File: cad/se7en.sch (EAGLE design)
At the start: 67 parts, among them CN1 MICROSD-EJECT, CN3 DO NOT PLACE, CN4 DO NOT PLACE, CN5 DO NOT PLACE, CN8 HEADER-1X2-THM, Q1 FDC6392S, SW1 SWITCHKMR211, SW2 SWITCHKMR211, U1 ATSAMS70, U2 MCP73831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

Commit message: tweak
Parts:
- CN2: device adafruit:JST_2PIN-SMT-RA -> jaw:JST_2PIN-SMT-RA
- USB1: value CON-USB-F-MICRO-B -> USB-F-B-MICRO-B-192; device dp_devices:CON-USB-F-MICRO-B -> jaw:USB-F-B-MICRO-B-192
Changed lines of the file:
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@@
 <grid distance="0.1" unitdist="inch" unit="inch" style="lines" multiple="1" display="no" altdistance="0.01" altunitdist="inch" altunit="inch"/>
 <layers>
-<layer number="1" name="Top" color="4" fill="1" visible="no" active="no"/>
-<layer number="2" name="Route2" color="6" fill="1" visible="no" active="no"/>
-<layer number="3" name="Route3" color="4" fill="3" visible="no" active="no"/>
-<layer number="14" name="Route14" color="1" fill="6" visible="no" active="no"/>
-<layer number="15" name="Route15" color="13" fill="1" visible="no" active="no"/>
-<layer number="16" name="Bottom" color="1" fill="1" visible="no" active="no"/>
-<layer number="17" name="Pads" color="2" fill="1" visible="no" active="no"/>
-<layer number="18" name="Vias" color="2" fill="1" visible="no" active="no"/>
-<layer number="19" name="Unrouted" color="6" fill="1" visible="no" active="no"/>
-<layer number="20" name="Dimension" color="15" fill="1" visible="no" active="no"/>
-<layer number="21" name="tPlace" color="7" fill="1" visible="no" active="no"/>
-<layer number="22" name="bPlace" color="7" fill="1" visible="no" active="no"/>
-<layer number="23" name="tOrigins" color="15" fill="1" visible="no" active="no"/>
-<layer number="24" name="bOrigins" color="15" fill="1" visible="no" active="no"/>
-<layer number="25" name="tNames" color="7" fill="1" visible="no" active="no"/>
-<layer number="26" name="bNames" color="7" fill="1" visible="no" active="no"/>
-<layer number="27" name="tValues" color="7" fill="1" visible="no" active="no"/>
-<layer number="28" name="bValues" color="7" fill="1" visible="no" active="no"/>
+<layer number="1" name="Top" color="4" fill="1" visible="yes" active="no"/>
+<layer number="2" name="Route2" color="6" fill="1" visible="yes" active="no"/>
+<layer number="3" name="Route3" color="4" fill="3" visible="yes" active="no"/>
+<layer number="14" name="Route14" color="1" fill="6" visible="yes" active="no"/>
+<layer number="15" name="Route15" color="13" fill="1" visible="yes" active="no"/>
+<layer number="16" name="Bottom" color="1" fill="1" visible="yes" active="no"/>
+<layer number="17" name="Pads" color="2" fill="1" visible="yes" active="no"/>
+<layer number="18" name="Vias" color="2" fill="1" visible="yes" active="no"/>
+<layer number="19" name="Unrouted" color="6" fill="1" visible="yes" active="no"/>
+<layer number="20" name="Dimension" color="15" fill="1" visible="yes" active="no"/>
+<layer number="21" name="tPlace" color="7" fill="1" visible="yes" active="no"/>
+<layer number="22" name="bPlace" color="7" fill="1" visible="yes" active="no"/>
+<layer number="23" name="tOrigins" color="15" fill="1" visible="yes" active="no"/>
+<layer number="24" name="bOrigins" color="15" fill="1" visible="yes" active="no"/>
+<layer number="25" name="tNames" color="7" fill="1" visible="yes" active="no"/>
+<layer number="26" name="bNames" color="7" fill="1" visible="yes" active="no"/>
+<layer number="27" name="tValues" color="7" fill="1" visible="yes" active="no"/>
+<layer number="28" name="bValues" color="7" fill="1" visible="yes" active="no"/>
 <layer number="29" name="tStop" color="7" fill="3" visible="no" active="no"/>
 <layer number="30" name="bStop" color="7" fill="6" visible="no" active="no"/>
@@
 <layer number="35" name="tGlue" color="7" fill="4" visible="no" active="no"/>
 <layer number="36" name="bGlue" color="7" fill="5" visible="no" active="no"/>
-<layer number="37" name="tTest" color="7" fill="1" visible="no" active="no"/>
-<layer number="38" name="bTest" color="7" fill="1" visible="no" active="no"/>
+<layer number="37" name="tTest" color="7" fill="1" visible="yes" active="no"/>
+<layer number="38" name="bTest" color="7" fill="1" visible="yes" active="no"/>
 <layer number="39" name="tKeepout" color="4" fill="11" visible="no" active="no"/>
 <layer number="40" name="bKeepout" color="1" fill="11" visible="no" active="no"/>
@@
 <layer number="44" name="Drills" color="7" fill="1" visible="no" active="no"/>
 <layer number="45" name="Holes" color="7" fill="1" visible="no" active="no"/>
-<layer number="46" name="Milling" color="3" fill="1" visible="no" active="no"/>
-<layer number="47" name="Measures" color="7" fill="1" visible="no" active="no"/>
-<layer number="48" name="Document" color="7" fill="1" visible="no" active="no"/>
-<layer number="49" name="Reference" color="7" fill="1" visible="no" active="no"/>
-<layer number="50" name="dxf" color="7" fill="1" visible="no" active="no"/>
-<layer number="51" name="tDocu" color="7" fill="1" visible="no" active="no"/>
-<layer number="52" name="bDocu" color="7" fill="1" visible="no" active="no"/>
-<layer number="53" name="tGND_GNDA" color="7" fill="1" visible="no" active="no"/>
-<layer number="54" name="bGND_GNDA" color="7" fill="1" visible="no" active="no"/>
-<layer number="56" name="wert" color="7" fill="1" visible="no" active="no"/>
-<layer number="57" name="tCAD" color="7" fill="1" visible="no" active="no"/>
-<layer number="59" name="tCarbon" color="7" fill="1" visible="no" active="no"/>
-<layer number="60" name="bCarbon" color="7" fill="1" visible="no" active="no"/>
+<layer number="46" name="Milling" color="3" fill="1" visible="yes" active="no"/>
+<layer number="47" name="Measures" color="7" fill="1" visible="yes" active="no"/>
+<layer number="48" name="Document" color="7" fill="1" visible="yes" active="no"/>
+<layer number="49" name="Reference" color="7" fill="1" visible="yes" active="no"/>
+<layer number="50" name="dxf" color="7" fill="1" visible="yes" active="no"/>
+<layer number="51" name="tDocu" color="7" fill="1" visible="yes" active="no"/>
+<layer number="52" name="bDocu" color="7" fill="1" visible="yes" active="no"/>
+<layer number="53" name="tGND_GNDA" color="7" fill="1" visible="yes" active="no"/>
+<layer number="54" name="bGND_GNDA" color="7" fill="1" visible="yes" active="no"/>
+<layer number="56" name="wert" color="7" fill="1" visible="yes" active="no"/>
+<layer number="57" name="tCAD" color="7" fill="1" visible="yes" active="no"/>
+<layer number="59" name="tCarbon" color="7" fill="1" visible="yes" active="no"/>
+<layer number="60" name="bCarbon" color="7" fill="1" visible="yes" active="no"/>
 <layer number="90" name="Modules" color="5" fill="1" visible="yes" active="yes"/>
 <layer number="91" name="Nets" color="2" fill="1" visible="yes" active="yes"/>
@@
 <part name="C17" library="jaw" deviceset="C" device="-0402" value=".1u"/>
 <part name="C18" library="jaw" deviceset="C" device="-0402" value=".1u"/>
-<part name="USB1" library="dp_devices" deviceset="CON-USB-F" device="-MICRO-B"/>
+<part name="USB1" library="jaw" deviceset="USB-F-B" device="-MICRO-B-192"/>
 <part name="GND10" library="jaw" deviceset="PWR-GND" device=""/>
 <part name="CN1" library="jaw" deviceset="MICROSD" device="-EJECT"/>
 <part name="C19" library="jaw" deviceset="C" device="-0402" value=".1u"/>
-<part name="CN2" library="adafruit" deviceset="JST_2PIN" device="-SMT-RA"/>
+<part name="CN2" library="jaw" deviceset="JST_2PIN" device="-SMT-RA"/>
 <part name="CN5" library="adafruit" deviceset="PINHD-2X20" device="" value="DO NOT PLACE"/>
 <part name="CN3" library="jaw" deviceset="HEADER-3X2" device="-POGO" value="DO NOT PLACE"/>

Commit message: usb improve Zd
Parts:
- CN8: value HEADER-1X2-THM -> HEADER-1X2M254; device jaw:HEADER-1X2-THM -> jaw:HEADER-1X2M254
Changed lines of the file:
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@@
 <part name="LED2" library="jaw" deviceset="LED" device="" value="green"/>
 <part name="LED3" library="jaw" deviceset="LED" device="" value="orange"/>
-<part name="CN8" library="jaw" deviceset="HEADER-1X2" device="-THM"/>
+<part name="CN8" library="jaw" deviceset="HEADER-1X2" device="M254" value="HEADER-1X2M254"/>
 </parts>
 <sheets>

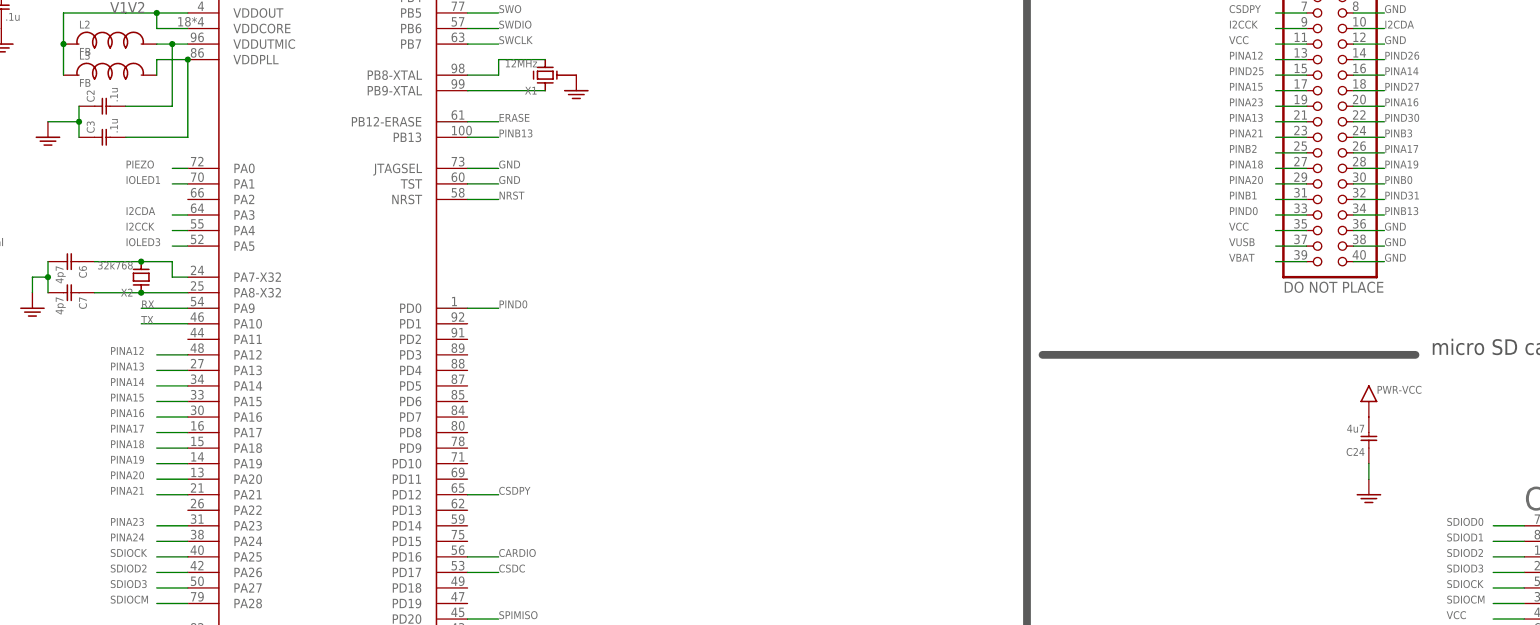
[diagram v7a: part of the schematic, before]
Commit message: drop vbat pins, add more io
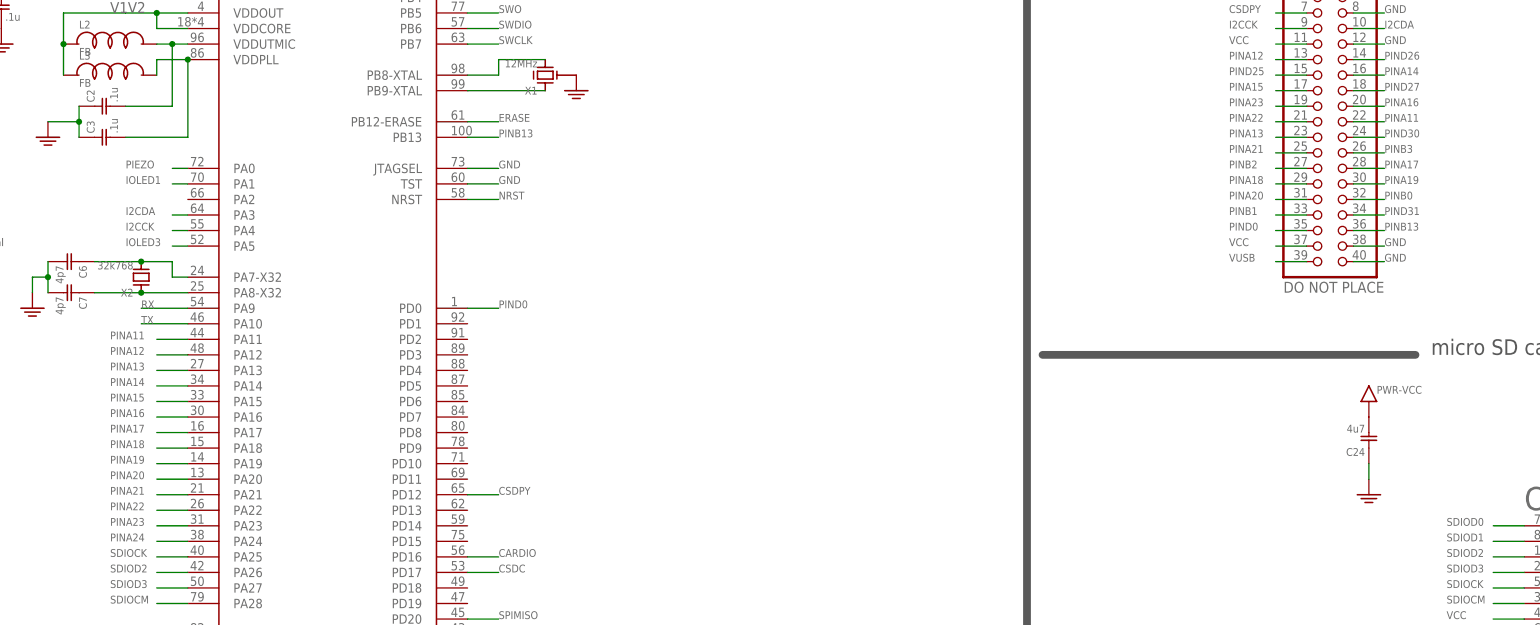
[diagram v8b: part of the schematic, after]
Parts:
- CN8: value HEADER-1X2M254 -> DO NOT PLACE
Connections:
- new net PINA11: CN5.22, U1.PA11
- new net PINA22: CN5.21, U1.PA22
- net GND: no longer CN5.36
- net PINA13: now also CN5.23; no longer CN5.21
- net PINA17: now also CN5.28; no longer CN5.26
- net PINA18: now also CN5.29; no longer CN5.27
- net PINA19: now also CN5.30; no longer CN5.28
- net PINA20: now also CN5.31; no longer CN5.29
- net PINA21: now also CN5.25; no longer CN5.23
- net PINB0: now also CN5.32; no longer CN5.30
- net PINB1: now also CN5.33; no longer CN5.31
- net PINB13: now also CN5.36; no longer CN5.34
- net PINB2: now also CN5.27; no longer CN5.25
- net PINB3: now also CN5.26; no longer CN5.24
- net PIND0: now also CN5.35; no longer CN5.33
- net PIND30: now also CN5.24; no longer CN5.22
- net PIND31: now also CN5.34; no longer CN5.32
- net VBAT: no longer CN5.39
- net VCC: now also CN5.37; no longer CN5.35
- net VUSB: now also CN5.39; no longer CN5.37
